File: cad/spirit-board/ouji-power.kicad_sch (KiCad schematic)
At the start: 2 parts, among them J36 SEEED lipo rider plus 1069902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, J38 BATTERY

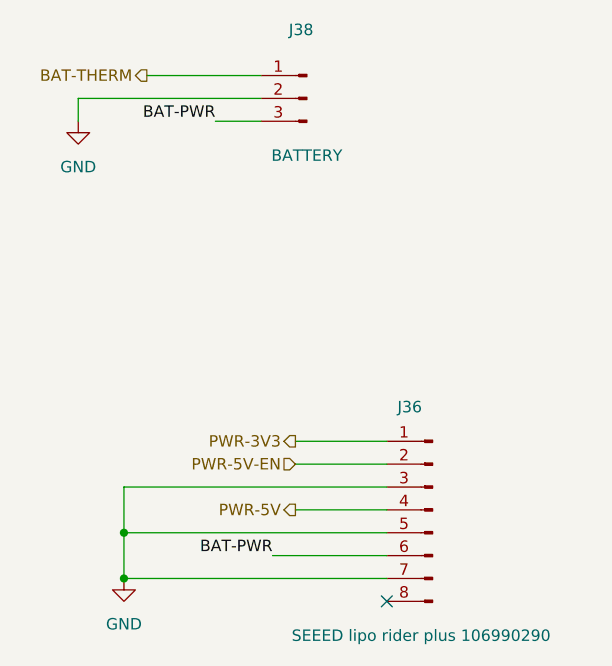
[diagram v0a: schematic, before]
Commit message: Mike's feedback
 - bypass caps on all power sources
 - Bulk cap on LED power
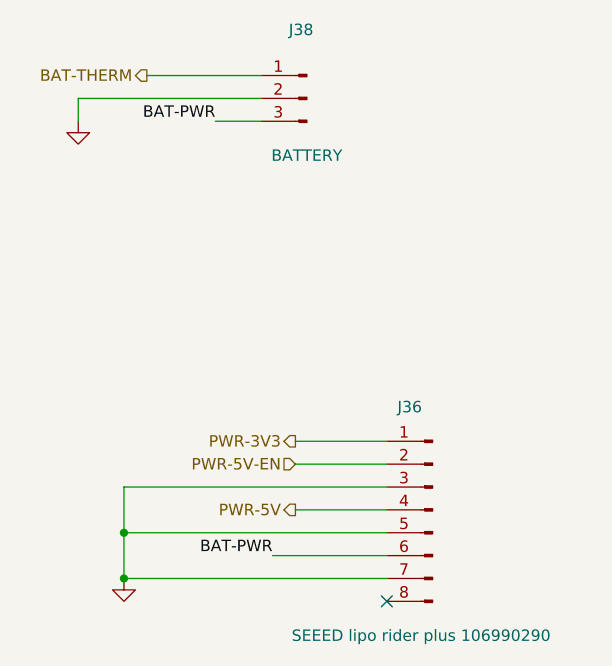
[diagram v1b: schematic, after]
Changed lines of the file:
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@@
     )
     (property "Value" "GND" (at 92.71 46.99 0)
-      (effects (font (size 1.27 1.27)))
+      (effects (font (size 1.27 1.27)) hide)
     )
     (property "Footprint" "" (at 92.71 41.91 0)
@@
     )
     (property "Value" "GND" (at 97.79 97.79 0)
-      (effects (font (size 1.27 1.27)))
+      (effects (font (size 1.27 1.27)) hide)
     )
     (property "Footprint" "" (at 97.79 92.71 0)
